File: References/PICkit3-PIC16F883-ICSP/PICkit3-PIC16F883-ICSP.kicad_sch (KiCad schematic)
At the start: 3 parts, among them J1 PICkit 3 ICSP, U1 PIC16F883 ICSP points

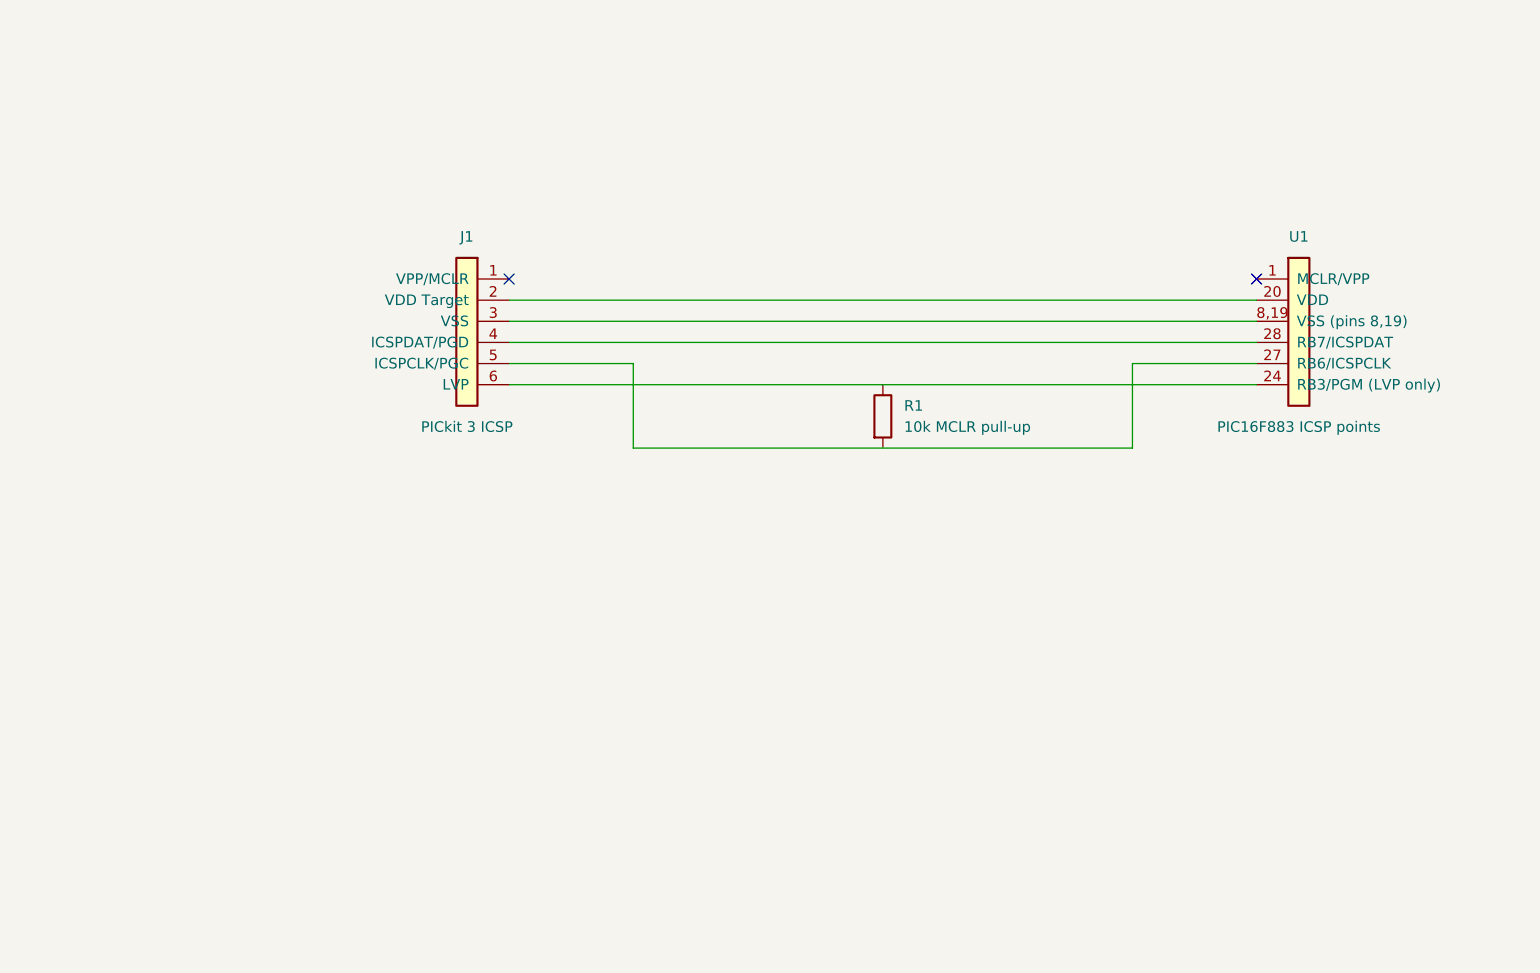
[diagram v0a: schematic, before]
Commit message: Simplify KiCad source to a parser-safe editable wiring diagram
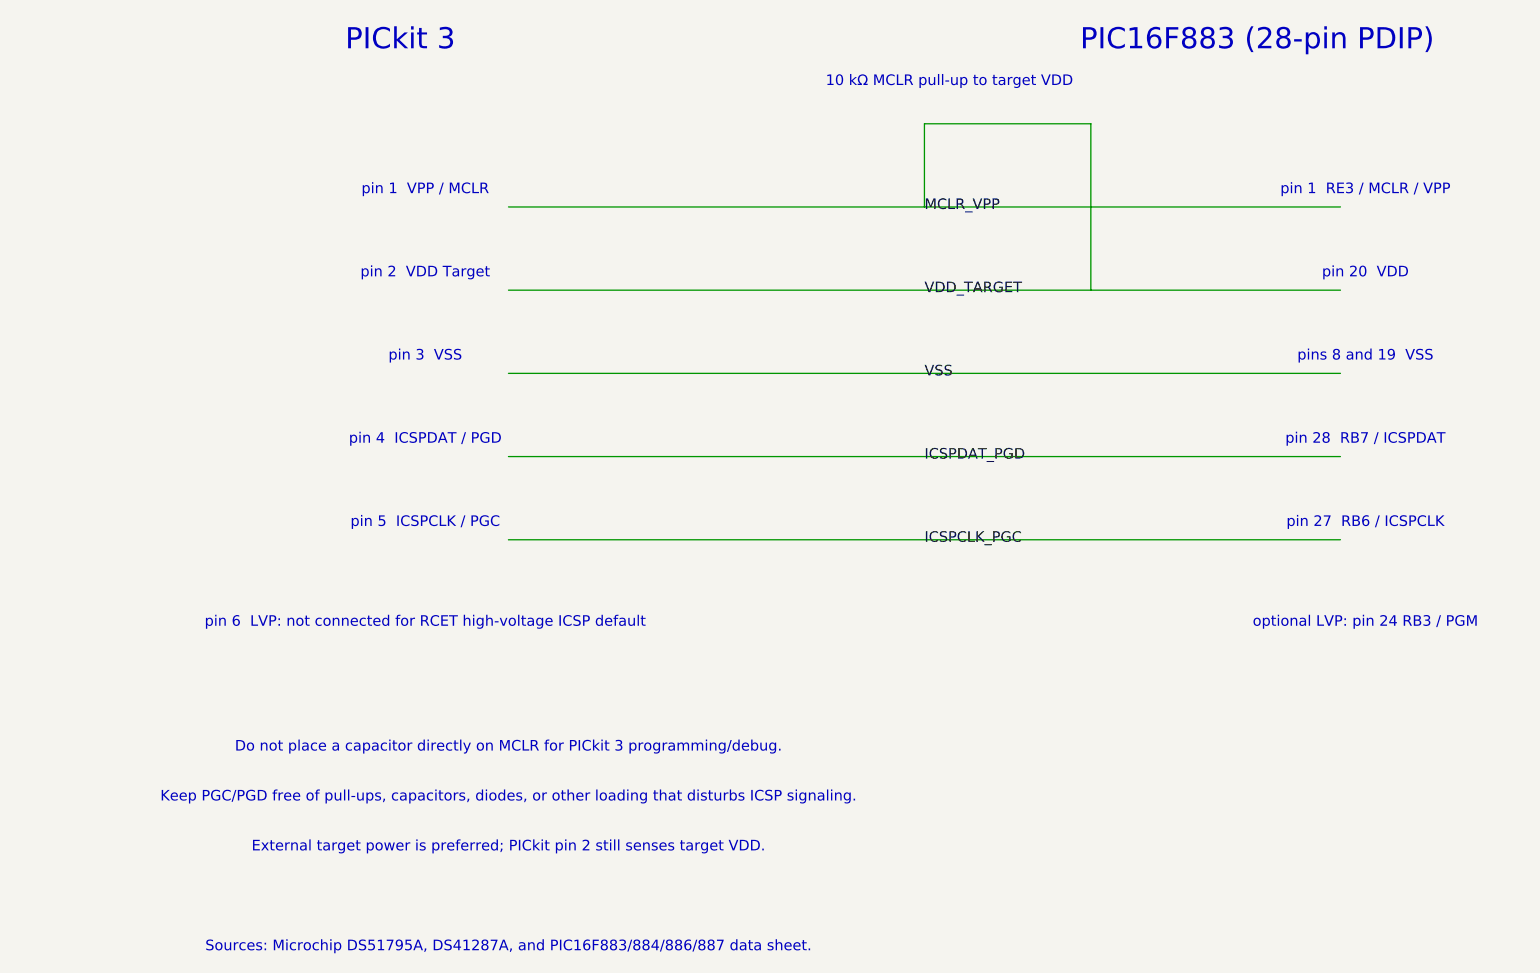
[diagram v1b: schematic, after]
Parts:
- removed J1: PICkit 3 ICSP, symbol RCET:PICkit3_ICSP
- removed R1: 10k MCLR pull-up, symbol Device:R
- removed U1: PIC16F883 ICSP points, Package_DIP:DIP-28_W7.62mm, symbol RCET:PIC16F883_ICSP
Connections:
- no-connect marks 2 -> 0
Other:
- note added: "10 kΩ MCLR pull-up to target VDD"
- note added: "Do not place a capacitor directly on MCLR for PICkit 3 programming/debug."
- note added: "External target power is preferred; PICkit pin 2 still senses target VDD."
- note added: "Keep PGC/PGD free of pull-ups, capacitors, diodes, or other loading that disturbs ICSP signaling."
- note added: "PIC16F883 (28-pin PDIP)"
- note added: "PICkit 3"
- note added: "Sources: Microchip DS51795A, DS41287A, and PIC16F883/884/886/887 data sheet."
- note added: "optional LVP: pin 24 RB3 / PGM"
- note added: "pin 1 RE3 / MCLR / VPP"
- note added: "pin 1 VPP / MCLR"
- note added: "pin 2 VDD Target"
- note added: "pin 20 VDD"
- note added: "pin 27 RB6 / ICSPCLK"
- note added: "pin 28 RB7 / ICSPDAT"
- note added: "pin 3 VSS"
- note added: "pin 4 ICSPDAT / PGD"
- note added: "pin 5 ICSPCLK / PGC"
- note added: "pin 6 LVP: not connected for RCET high-voltage ICSP default"
- note added: "pins 8 and 19 VSS"
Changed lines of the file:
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@@
-(kicad_sch (version 20230121) (generator eeschema)
+(kicad_sch (version 20230121) (generator openai_rcet)
   (paper "A4")
   (title_block
@@
     (comment 2 "High-voltage ICSP course default; LVP disabled")
   )
-  (wire (pts (xy 55.08 86.36) (xy 144.92 86.36))
+  (wire
+    (pts (xy 55 65) (xy 155 65))
     (stroke (width 0) (type default))
   )
-  (wire (pts (xy 55.08 83.82) (xy 70 83.82) (xy 70 93.98) (xy 130 93.98) (xy 130 83.82) (xy 144.92 83.82))
+  (wire
+    (pts (xy 55 75) (xy 155 75))
     (stroke (width 0) (type default))
   )
-  (wire (pts (xy 55.08 81.28) (xy 144.92 81.28))
+  (wire
+    (pts (xy 55 85) (xy 155 85))
     (stroke (width 0) (type default))
   )
-  (wire (pts (xy 55.08 78.74) (xy 144.92 78.74))
+  (wire
+    (pts (xy 55 95) (xy 155 95))
     (stroke (width 0) (type default))
   )
-  (wire (pts (xy 55.08 76.20) (xy 144.92 76.20))
+  (wire
+    (pts (xy 55 105) (xy 155 105))
     (stroke (width 0) (type default))
   )
-  (no_connect (at 55.08 73.66))
-  (no_connect (at 144.92 73.66))
-  (symbol (lib_id "RCET:PICkit3_ICSP") (at 50 80.01 0) (mirror y) (unit 1)
-    (in_bom yes) (on_board yes) (dnp no)
-    (property "Reference" "J1" (at 50 68.58 0)
-      (effects (font (size 1.27 1.27)))
-    )
-    (property "Value" "PICkit 3 ICSP" (at 50 91.44 0)
-      (effects (font (size 1.27 1.27)))
-    )
-    (property "Footprint" "" (at 50 80.01 0)
-      (effects (font (size 1.27 1.27)) hide)
-    )
-    (property "Datasheet" "Microchip DS51795A" (at 50 80.01 0)
-      (effects (font (size 1.27 1.27)) hide)
-    )
-    (pin "1")
-    (pin "2")
-    (pin "3")
-    (pin "4")
-    (pin "5")
-    (pin "6")
-    (instances
-      (project "PICkit3-PIC16F883-ICSP"
-        (path "/49122f3a-e33d-44f0-9255-b46f34ecb458"
-          (reference "J1") (unit 1)
-        )
-      )
-    )
+  (wire
+    (pts (xy 105 65) (xy 105 55) (xy 125 55) (xy 125 75))
+    (stroke (width 0) (type default))
   )
-  (symbol (lib_id "RCET:PIC16F883_ICSP") (at 150 80.01 0) (unit 1)
-    (in_bom yes) (on_board yes) (dnp no)
-    (property "Reference" "U1" (at 150 68.58 0)
-      (effects (font (size 1.27 1.27)))
-    )
-    (property "Value" "PIC16F883 ICSP points" (at 150 91.44 0)
-      (effects (font (size 1.27 1.27)))
-    )
-    (property "Footprint" "Package_DIP:DIP-28_W7.62mm" (at 150 80.01 0)
-      (effects (font (size 1.27 1.27)) hide)
-    )
-    (property "Datasheet" "Microchip DS40001291H / DS41287A" (at 150 80.01 0)
-      (effects (font (size 1.27 1.27)) hide)
-    )
-    (pin "1")
-    (pin "20")
-    (pin "8,19")
-    (pin "28")
-    (pin "27")
-    (pin "24")
-    (instances
-      (project "PICkit3-PIC16F883-ICSP"
-        (path "/49122f3a-e33d-44f0-9255-b46f34ecb458"
-          (reference "U1") (unit 1)
-        )
-      )
-    )
+  (label "MCLR_VPP"
+    (at 105 65 0)
+    (effects (font (size 1.27 1.27)))
   )
-  (symbol (lib_id "Device:R") (at 100 90.17 0) (unit 1)
-    (in_bom yes) (on_board yes) (dnp no)
-    (property "Reference" "R1" (at 102.54 88.9 0)
-      (effects (font (size 1.27 1.27)) (justify left))
-    )
-    (property "Value" "10k MCLR pull-up" (at 102.54 91.44 0)
-      (effects (font (size 1.27 1.27)) (justify left))
-    )
-    (property "Footprint" "" (at 98.222 90.17 90)
-      (effects (font (size 1.27 1.27)) hide)
-    )
-    (property "Datasheet" "Microchip DS51795A" (at 100 90.17 0)
-      (effects (font (size 1.27 1.27)) hide)
-    )
-    (pin "1")
-    (pin "2")
-    (instances
-      (project "PICkit3-PIC16F883-ICSP"
-        (path "/49122f3a-e33d-44f0-9255-b46f34ecb458"
-          (reference "R1") (unit 1)
-        )
-      )
-    )
+  (label "VDD_TARGET"
+    (at 105 75 0)
+    (effects (font (size 1.27 1.27)))
+  )
+  (label "VSS"
+    (at 105 85 0)
+    (effects (font (size 1.27 1.27)))
+  )
+  (label "ICSPDAT_PGD"
+    (at 105 95 0)
+    (effects (font (size 1.27 1.27)))
+  )
+  (label "ICSPCLK_PGC"
+    (at 105 105 0)
+    (effects (font (size 1.27 1.27)))
+  )
+  (text "PICkit 3"
+    (at 42 45 0)
+    (effects (font (size 2.54 2.54)))
+  )
+  (text "PIC16F883 (28-pin PDIP)"
+    (at 145 45 0)
+    (effects (font (size 2.54 2.54)))
+  )
+  (text "pin 1  VPP / MCLR"
+    (at 45 63 0)
+    (effects (font (size 1.27 1.27)))
+  )
+  (text "pin 2  VDD Target"
+    (at 45 73 0)
+    (effects (font (size 1.27 1.27)))
+  )
+  (text "pin 3  VSS"
+    (at 45 83 0)
+    (effects (font (size 1.27 1.27)))
+  )
+  (text "pin 4  ICSPDAT / PGD"
+    (at 45 93 0)
+    (effects (font (size 1.27 1.27)))
+  )
+  (text "pin 5  ICSPCLK / PGC"
+    (at 45 103 0)
+    (effects (font (size 1.27 1.27)))
+  )
+  (text "pin 6  LVP: not connected for RCET high-voltage ICSP default"
+    (at 45 115 0)
+    (effects (font (size 1.27 1.27)))
+  )
+  (text "pin 1  RE3 / MCLR / VPP"
+    (at 158 63 0)
+    (effects (font (size 1.27 1.27)))
+  )
+  (text "pin 20  VDD"
+    (at 158 73 0)
+    (effects (font (size 1.27 1.27)))
+  )
+  (text "pins 8 and 19  VSS"
+    (at 158 83 0)
+    (effects (font (size 1.27 1.27)))
+  )
+  (text "pin 28  RB7 / ICSPDAT"
+    (at 158 93 0)
+    (effects (font (size 1.27 1.27)))
+  )
+  (text "pin 27  RB6 / ICSPCLK"
+    (at 158 103 0)
+    (effects (font (size 1.27 1.27)))
+  )
+  (text "optional LVP: pin 24 RB3 / PGM"
+    (at 158 115 0)
+    (effects (font (size 1.27 1.27)))
+  )
+  (text "10 kΩ MCLR pull-up to target VDD"
+    (at 108 50 0)
+    (effects (font (size 1.27 1.27)))
+  )
+  (text "Do not place a capacitor directly on MCLR for PICkit 3 programming/debug."
+    (at 55 130 0)
+    (effects (font (size 1.27 1.27)))
+  )
+  (text "Keep PGC/PGD free of pull-ups, capacitors, diodes, or other loading that disturbs ICSP signaling."
+    (at 55 136 0)
+    (effects (font (size 1.27 1.27)))
+  )
+  (text "External target power is preferred; PICkit pin 2 still senses target VDD."
+    (at 55 142 0)
+    (effects (font (size 1.27 1.27)))
+  )
+  (text "Sources: Microchip DS51795A, DS41287A, and PIC16F883/884/886/887 data sheet."
+    (at 55 154 0)
+    (effects (font (size 1.27 1.27)))
   )
   (sheet_instances
